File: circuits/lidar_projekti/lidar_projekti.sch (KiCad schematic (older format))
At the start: 1 part

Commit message: [PATCH] Updated KiCAD files
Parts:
- added D?: LED_GRBC, symbol Device:LED_GRBC
- added J?: Conn_01x04, symbol Connector_Generic:Conn_01x04
- added R? (x4): R, symbol Device:R
- added SW?: SW_Push_Open, symbol Switch:SW_Push_Open
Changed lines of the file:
@@
+	1    0    0    -1
+$EndComp
+$Comp
+L Device:LED_GRBC D?
+U 1 1 6230AA77
+P 4450 3500
+F 0 "D?" H 4450 3997 50  0000 C CNN
+F 1 "LED_GRBC" H 4450 3906 50  0000 C CNN
+F 2 "" H 4450 3450 50  0001 C CNN
+F 3 "~" H 4450 3450 50  0001 C CNN
+	1    4450 3500
+	1    0    0    -1
+$EndComp
+$Comp
+L Switch:SW_Push_Open SW?
+U 1 1 6230BF01
+P 4500 4550
+F 0 "SW?" H 4500 4765 50  0000 C CNN
+F 1 "SW_Push_Open" H 4500 4674 50  0000 C CNN
+F 2 "" H 4500 4750 50  0001 C CNN
+F 3 "~" H 4500 4750 50  0001 C CNN
+	1    4500 4550
+	1    0    0    -1
+$EndComp
+$Comp
+L Device:R R?
+U 1 1 6230C6DA
+P 7450 3550
+F 0 "R?" H 7520 3596 50  0000 L CNN
+F 1 "R" H 7520 3505 50  0000 L CNN
+F 2 "" V 7380 3550 50  0001 C CNN
+F 3 "~" H 7450 3550 50  0001 C CNN
+	1    7450 3550
+	1    0    0    -1
+$EndComp
+$Comp
+L Device:R R?
+U 1 1 6230CE1C
+P 7450 4050
+F 0 "R?" H 7520 4096 50  0000 L CNN
+F 1 "R" H 7520 4005 50  0000 L CNN
+F 2 "" V 7380 4050 50  0001 C CNN
+F 3 "~" H 7450 4050 50  0001 C CNN
+	1    7450 4050
+	1    0    0    -1
+$EndComp
+$Comp
+L Device:R R?
+U 1 1 6230CFB6
+P 7450 4550
+F 0 "R?" H 7520 4596 50  0000 L CNN
+F 1 "R" H 7520 4505 50  0000 L CNN
+F 2 "" V 7380 4550 50  0001 C CNN
+F 3 "~" H 7450 4550 50  0001 C CNN
+	1    7450 4550
+	1    0    0    -1
+$EndComp
+$Comp
+L Connector_Generic:Conn_01x04 J?
+U 1 1 6230D64D
+P 6000 2600
+F 0 "J?" H 6080 2592 50  0000 L CNN
+F 1 "Conn_01x04" H 6080 2501 50  0000 L CNN
+F 2 "" H 6000 2600 50  0001 C CNN
+F 3 "~" H 6000 2600 50  0001 C CNN
+	1    6000 2600
+	1    0    0    -1
+$EndComp
+$Comp
+L Device:R R?
+U 1 1 6230DED0
+P 7450 5050
+F 0 "R?" H 7520 5096 50  0000 L CNN
+F 1 "R" H 7520 5005 50  0000 L CNN
+F 2 "" V 7380 5050 50  0001 C CNN
+F 3 "~" H 7450 5050 50  0001 C CNN
+	1    7450 5050
 	1    0    0    -1
 $EndComp

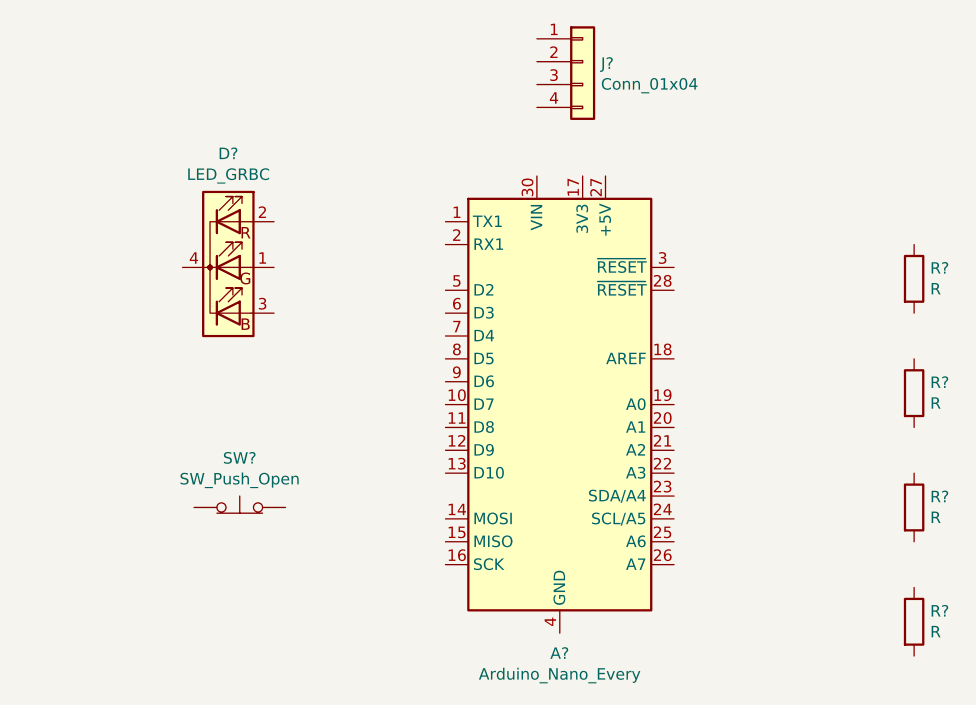
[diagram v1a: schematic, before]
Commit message: [PATCH] Fixed electrical errors
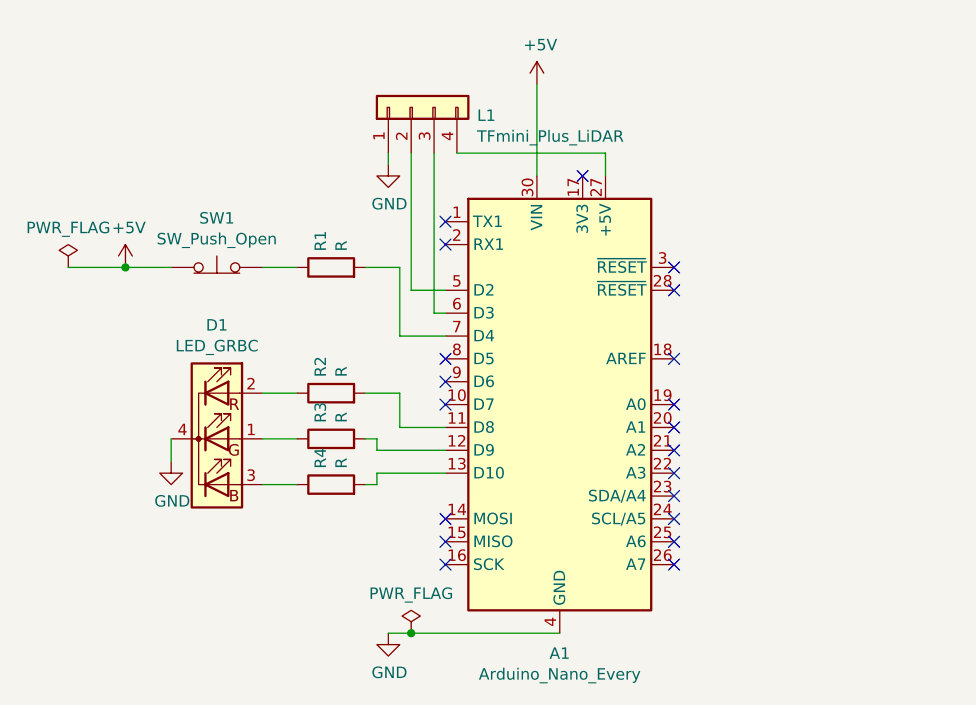
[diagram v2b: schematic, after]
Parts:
- L1: renamed from J?; value Conn_01x04 -> TFmini_Plus_LiDAR
- gave numbers to parts that had none: 7
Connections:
- net at A1.11 (D8): now also R2.2
- net at A1.12 (D9): now also R3.2
- net at A1.13 (D10): now also R4.2
- net at A1.27 (+5V): now also L1.4 (Pin_4)
- net GND: now reaches A1.29 (GND), A1.4 (GND)
- net GND: now also D1.4 (K), L1.1 (Pin_1)
- net +5V: now reaches A1.30 (VIN)
- net +5V: now also SW1.1 (A)
- net at A1.5 (D2): now also L1.2 (Pin_2)
- net at A1.6 (D3): now also L1.3 (Pin_3)
- net at A1.7 (D4): now also R1.2
- net at D1.1 (GA): now also R3.1
- net at D1.2 (RA): now also R2.1
- net at D1.3 (BA): now also R4.1
- net at SW1.2 (B): now also R1.1
- no-connect marks 0 -> 20
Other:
- moved on the sheet: D1, L1, R1, R2, R3, R4, SW1

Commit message: [PATCH] Added PCB schematics
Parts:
- removed SW1: SW_Push_Open, symbol Switch:SW_Push_Open
- added SW2: SW_SPDT, Button_Switch_SMD:SW_SPST_B3S-1100, symbol Switch:SW_SPDT
- D1: footprint (none) -> LED_SMD:LED_ASMB-KTF0-0A306
- L1: footprint (none) -> Connector:FanPinHeader_1x04_P2.54mm_Vertical
- R1: footprint (none) -> Resistor_THT:R_Axial_DIN0309_L9.0mm_D3.2mm_P12.70mm_Horizontal
- R2: value R -> 180R; footprint (none) -> Resistor_THT:R_Axial_DIN0309_L9.0mm_D3.2mm_P12.70mm_Horizontal
- R3, R4: value R -> 120R; footprint (none) -> Resistor_THT:R_Axial_DIN0309_L9.0mm_D3.2mm_P12.70mm_Horizontal
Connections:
- net +5V: now also SW2.2 (B)
- net GND: now also R1.2
- net at A1.7 (D4): now also SW2.3 (C); no longer R1.2
- net at R1.1: now also SW2.1 (A)
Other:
- moved on the sheet: R1
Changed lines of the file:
@@
 F 0 "D1" H 4400 4747 50  0000 C CNN
 F 1 "LED_GRBC" H 4400 4656 50  0000 C CNN
-F 2 "" H 4400 4200 50  0001 C CNN
+F 2 "LED_SMD:LED_ASMB-KTF0-0A306" H 4400 4200 50  0001 C CNN
 F 3 "~" H 4400 4200 50  0001 C CNN
 	1    4400 4250
-	1    0    0    -1
-$EndComp
-$Comp
-L Switch:SW_Push_Open SW1
-U 1 1 6230BF01
-P 4400 3500
-F 0 "SW1" H 4400 3715 50  0000 C CNN
-F 1 "SW_Push_Open" H 4400 3624 50  0000 C CNN
-F 2 "" H 4400 3700 50  0001 C CNN
-F 3 "~" H 4400 3700 50  0001 C CNN
-	1    4400 3500
 	1    0    0    -1
 $EndComp
@@
 U 1 1 6230C6DA
 P 4900 4050
-F 0 "R2" H 4970 4096 50  0000 L CNN
-F 1 "R" H 4970 4005 50  0000 L CNN
-F 2 "" V 4830 4050 50  0001 C CNN
+F 0 "R2" V 5107 4050 50  0000 C CNN
+F 1 "180R" V 5016 4050 50  0000 C CNN
+F 2 "Resistor_THT:R_Axial_DIN0309_L9.0mm_D3.2mm_P12.70mm_Horizontal" V 4830 4050 50  0001 C CNN
 F 3 "~" H 4900 4050 50  0001 C CNN
 	1    4900 4050
@@
 U 1 1 6230CE1C
 P 4900 4250
-F 0 "R3" H 4970 4296 50  0000 L CNN
-F 1 "R" H 4970 4205 50  0000 L CNN
-F 2 "" V 4830 4250 50  0001 C CNN
+F 0 "R3" V 5107 4250 50  0000 C CNN
+F 1 "120R" V 5016 4250 50  0000 C CNN
+F 2 "Resistor_THT:R_Axial_DIN0309_L9.0mm_D3.2mm_P12.70mm_Horizontal" V 4830 4250 50  0001 C CNN
 F 3 "~" H 4900 4250 50  0001 C CNN
 	1    4900 4250
@@
 U 1 1 6230CFB6
 P 4900 4450
-F 0 "R4" H 4970 4496 50  0000 L CNN
-F 1 "R" H 4970 4405 50  0000 L CNN
-F 2 "" V 4830 4450 50  0001 C CNN
+F 0 "R4" V 5107 4450 50  0000 C CNN
+F 1 "120R" V 5016 4450 50  0000 C CNN
+F 2 "Resistor_THT:R_Axial_DIN0309_L9.0mm_D3.2mm_P12.70mm_Horizontal" V 4830 4450 50  0001 C CNN
 F 3 "~" H 4900 4450 50  0001 C CNN
 	1    4900 4450
@@
 F 0 "L1" V 5214 2512 50  0000 R CNN
 F 1 "TFmini_Plus_LiDAR" V 5123 2512 50  0000 R CNN
-F 2 "" H 5250 2800 50  0001 C CNN
+F 2 "Connector:FanPinHeader_1x04_P2.54mm_Vertical" H 5250 2800 50  0001 C CNN
 F 3 "~" H 5250 2800 50  0001 C CNN
 	1    5250 2800
@@
 L Device:R R1
 U 1 1 6230DED0
-P 4900 3500
-F 0 "R1" H 4970 3546 50  0000 L CNN
-F 1 "R" H 4970 3455 50  0000 L CNN
-F 2 "" V 4830 3500 50  0001 C CNN
-F 3 "~" H 4900 3500 50  0001 C CNN
-	1    4900 3500
+P 4650 2950
+F 0 "R1" H 4720 2996 50  0000 L CNN
+F 1 "R" H 4720 2905 50  0000 L CNN
+F 2 "Resistor_THT:R_Axial_DIN0309_L9.0mm_D3.2mm_P12.70mm_Horizontal" V 4580 2950 50  0001 C CNN
+F 3 "~" H 4650 2950 50  0001 C CNN
+	1    4650 2950
 	0    -1   -1   0
 $EndComp
@@
 Wire Wire Line
 	5200 3800 5200 3500
-Wire Wire Line
-	5200 3500 5050 3500
-Wire Wire Line
-	4750 3500 4600 3500
 Wire Wire Line
 	6100 3000 6100 3100
@@
 L power:+5V #PWR0105
 U 1 1 623269DC
-P 4000 3500
-F 0 "#PWR0105" H 4000 3350 50  0001 C CNN
-F 1 "+5V" H 4015 3673 50  0000 C CNN
-F 2 "" H 4000 3500 50  0001 C CNN
-F 3 "" H 4000 3500 50  0001 C CNN
-	1    4000 3500
-	1    0    0    -1
-$EndComp
-Wire Wire Line
-	4200 3500 4000 3500
-$Comp
-L power:PWR_FLAG #FLG0102
-U 1 1 62328889
-P 3750 3500
-F 0 "#FLG0102" H 3750 3575 50  0001 C CNN
-F 1 "PWR_FLAG" H 3750 3673 50  0000 C CNN
-F 2 "" H 3750 3500 50  0001 C CNN
-F 3 "~" H 3750 3500 50  0001 C CNN
-	1    3750 3500
-	1    0    0    -1
-$EndComp
-Wire Wire Line
-	3750 3500 4000 3500
-Connection ~ 4000 3500
+P 3950 3400
+F 0 "#PWR0105" H 3950 3250 50  0001 C CNN
+F 1 "+5V" H 3965 3573 50  0000 C CNN
+F 2 "" H 3950 3400 50  0001 C CNN
+F 3 "" H 3950 3400 50  0001 C CNN
+	1    3950 3400
+	1    0    0    -1
+$EndComp
 $Comp
 L power:PWR_FLAG #FLG0104
@@
 Wire Wire Line
 	5800 2700 5800 3100
+Wire Wire Line
+	3700 3400 3950 3400
+$Comp
+L power:PWR_FLAG #FLG0102
+U 1 1 62328889
+P 3700 3400
+F 0 "#FLG0102" H 3700 3475 50  0001 C CNN
+F 1 "PWR_FLAG" H 3700 3573 50  0000 C CNN
+F 2 "" H 3700 3400 50  0001 C CNN
+F 3 "~" H 3700 3400 50  0001 C CNN
+	1    3700 3400
+	1    0    0    -1
+$EndComp
+$Comp
+L Switch:SW_SPDT SW2
+U 1 1 6233E6FF
+P 4300 3400
+F 0 "SW2" H 4300 3685 50  0000 C CNN
+F 1 "SW_SPDT" H 4300 3594 50  0000 C CNN
+F 2 "Button_Switch_SMD:SW_SPST_B3S-1100" H 4300 3400 50  0001 C CNN
+F 3 "~" H 4300 3400 50  0001 C CNN
+	1    4300 3400
+	1    0    0    -1
+$EndComp
+$Comp
+L power:GND #PWR01
+U 1 1 6234526F
+P 4800 3050
+F 0 "#PWR01" H 4800 2800 50  0001 C CNN
+F 1 "GND" H 4805 2877 50  0000 C CNN
+F 2 "" H 4800 3050 50  0001 C CNN
+F 3 "" H 4800 3050 50  0001 C CNN
+	1    4800 3050
+	1    0    0    -1
+$EndComp
+Wire Wire Line
+	4800 2950 4800 3050
+Wire Wire Line
+	4500 3300 4500 2950
+Wire Wire Line
+	4100 3400 3950 3400
+Connection ~ 3950 3400
+Wire Wire Line
+	4500 3500 5200 3500
 $EndSCHEMATC

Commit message: [PATCH] Added 10k resistor value
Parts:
- R1: value R -> 10k
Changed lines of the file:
@@
 U 1 1 6230DED0
 P 4650 2950
-F 0 "R1" H 4720 2996 50  0000 L CNN
-F 1 "R" H 4720 2905 50  0000 L CNN
+F 0 "R1" V 4857 2950 50  0000 C CNN
+F 1 "10k" V 4766 2950 50  0000 C CNN
 F 2 "Resistor_THT:R_Axial_DIN0309_L9.0mm_D3.2mm_P12.70mm_Horizontal" V 4580 2950 50  0001 C CNN
 F 3 "~" H 4650 2950 50  0001 C CNN

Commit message: [PATCH] Screenshots
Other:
- note added: "1.0\n"
- note added: "2022/03/15"
- note added: "LiDAR-Projekti"
- moved on the sheet: A1, D1, L1, R1, R2, R3, R4, SW2
